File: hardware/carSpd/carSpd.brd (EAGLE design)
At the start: 68.5 x 32.5 mm, 66 parts, among them IC1 MCP16301/H, IC2 CP2102, IC3 DS3231/SO, Q1 2n3904, U1 ATMEGA328P_TQFP, U3 ERC1602-4SMD-LED, U4 DS1820, Y1 16mhz, Y2 16MHZ

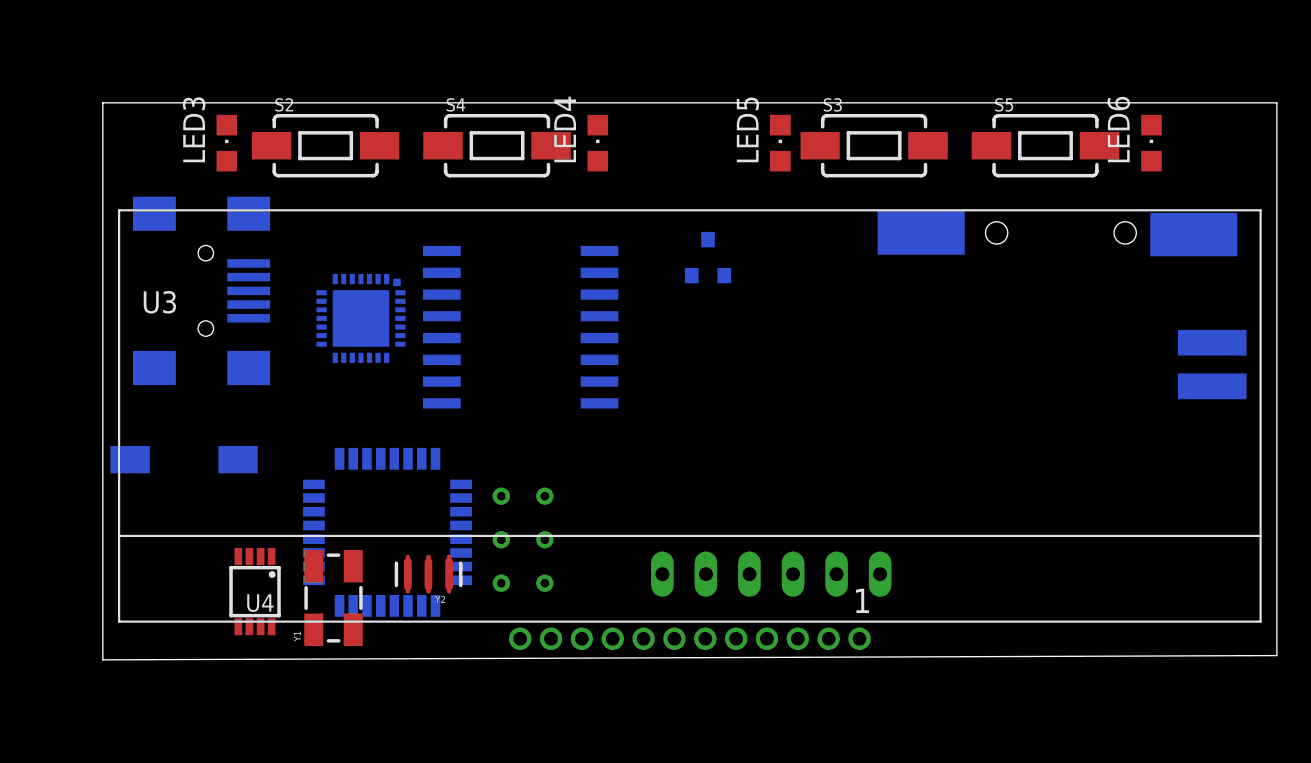
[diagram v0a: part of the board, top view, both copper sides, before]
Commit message: Corrected and verified schematics
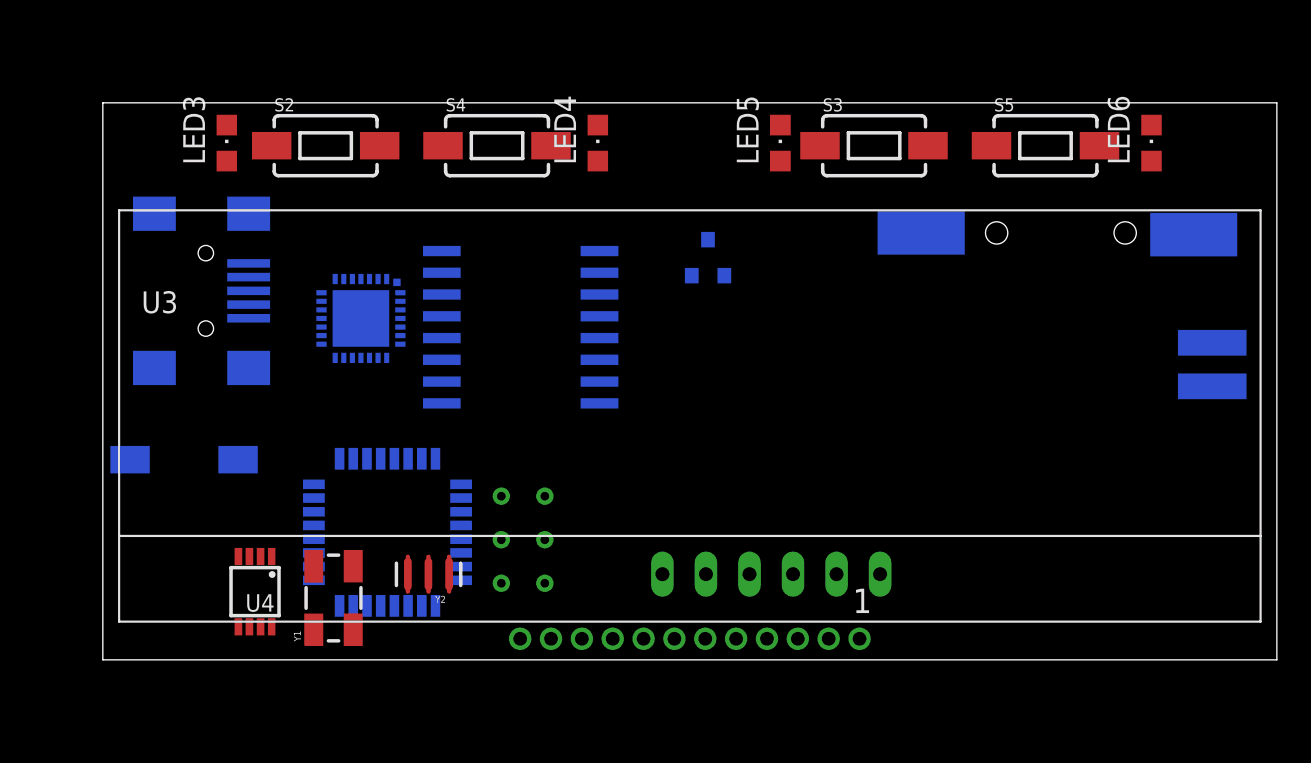
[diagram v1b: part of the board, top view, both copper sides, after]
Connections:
- removed net N$23: LED3.A, LED4.A, LED5.A, LED6.A, R15.1
- removed net N$25: C7.2, IC1.3, R8.1, R9.1
- new net N$1: IC1.3, R8.1, R9.1
- new net N$2: LED3.C, LED4.C, LED5.C, LED6.C, R15.1
- net +5V: now also LED3.A, LED4.A, LED5.A, LED6.A, U3.LED+
- net GND: now also C7.2; no longer LED3.C, LED4.C, LED5.C, LED6.C, U3.LED-
- net N$16: now also U3.LED-; no longer U3.LED+
- net TEMP: now also U1.14
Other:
- outline, holes or cut-outs redrawn
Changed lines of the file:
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@@
 <board>
 <plain>
-<wire x1="0" y1="0" x2="68.5" y2="0.25" width="0" layer="20"/>
-<wire x1="68.5" y1="0.25" x2="68.5" y2="32.5" width="0" layer="20"/>
+<wire x1="0" y1="0" x2="68.5" y2="0" width="0" layer="20"/>
+<wire x1="68.5" y1="0" x2="68.5" y2="32.5" width="0" layer="20"/>
 <wire x1="68.5" y1="32.5" x2="0" y2="32.5" width="0" layer="20"/>
 <wire x1="0" y1="32.5" x2="0" y2="0" width="0" layer="20"/>
@@
 <contactref element="C8" pad="2"/>
 <contactref element="U4" pad="4"/>
-<contactref element="LED3" pad="C"/>
-<contactref element="LED4" pad="C"/>
-<contactref element="LED5" pad="C"/>
-<contactref element="LED6" pad="C"/>
 <contactref element="IC3" pad="13"/>
 <contactref element="IC3" pad="5"/>
@@
 <contactref element="U3" pad="10"/>
 <contactref element="U3" pad="6"/>
-<contactref element="U3" pad="LED-"/>
 <contactref element="C4" pad="1"/>
 <contactref element="SV1" pad="6"/>
 <contactref element="IC1" pad="2"/>
-<contactref element="R8" pad="2"/>
 <contactref element="D4" pad="A"/>
 <contactref element="C5" pad="2"/>
@@
 <contactref element="D8" pad="A"/>
 <contactref element="U2" pad="1"/>
+<contactref element="C7" pad="2"/>
+<contactref element="R8" pad="2"/>
 <wire x1="-116" y1="-85" x2="-122" y2="-85" width="0" layer="19" extent="1-1"/>
 <wire x1="-110" y1="-85" x2="-116" y2="-85" width="0" layer="19" extent="1-1"/>
@@
 <wire x1="-101.85" y1="-70" x2="-104.3114" y2="-81.0988" width="0" layer="19" extent="1-1"/>
 <wire x1="-98.15" y1="-53" x2="-101.85" y2="-70" width="0" layer="19" extent="1-1"/>
-<wire x1="-99" y1="-36.15" x2="-98.15" y2="-53" width="0" layer="19" extent="1-1"/>
+<wire x1="-98.125" y1="-48" x2="-98.15" y2="-53" width="0" layer="19" extent="1-1"/>
+<wire x1="-99" y1="-36.15" x2="-98.125" y2="-48" width="0" layer="19" extent="1-1"/>
 <wire x1="-70.3" y1="-18.58" x2="-99" y2="-36.15" width="0" layer="19" extent="1-1"/>
 <wire x1="-56.18" y1="-13.42" x2="-70.3" y2="-18.58" width="0" layer="19" extent="1-1"/>
@@
 <wire x1="16.15" y1="30" x2="19.78" y2="23.855" width="0" layer="19" extent="1-16"/>
 <wire x1="8.51" y1="23.13" x2="15.06" y2="19.92" width="0" layer="19" extent="16-16"/>
-<wire x1="7.23" y1="31.2" x2="8.51" y2="23.13" width="0" layer="19" extent="1-16"/>
 <wire x1="26.15" y1="30" x2="19.78" y2="23.855" width="0" layer="19" extent="1-16"/>
-<wire x1="28.88" y1="31.2" x2="26.15" y2="30" width="0" layer="19" extent="1-1"/>
 <wire x1="28.98" y1="23.855" x2="26.15" y2="30" width="0" layer="19" extent="1-16"/>
 <wire x1="28.98" y1="22.585" x2="28.98" y2="23.855" width="0" layer="19" extent="16-16"/>
@@
 <wire x1="28.98" y1="18.775" x2="28.98" y2="20.045" width="0" layer="19" extent="16-16"/>
 <wire x1="34.36" y1="22.42" x2="28.98" y2="22.585" width="0" layer="19" extent="16-16"/>
-<wire x1="39.53" y1="31.2" x2="34.36" y2="22.42" width="0" layer="19" extent="1-16"/>
-<wire x1="48.15" y1="30" x2="39.53" y2="31.2" width="0" layer="19" extent="1-1"/>
+<wire x1="48.15" y1="30" x2="34.36" y2="22.42" width="0" layer="19" extent="1-16"/>
 <wire x1="58.15" y1="30" x2="48.15" y2="30" width="0" layer="19" extent="1-1"/>
-<wire x1="61.18" y1="31.2" x2="58.15" y2="30" width="0" layer="19" extent="1-1"/>
-<wire x1="63.65" y1="24.81" x2="61.18" y2="31.2" width="0" layer="19" extent="1-16"/>
-<wire x1="64.73" y1="15.96" x2="63.65" y2="24.81" width="0" layer="19" extent="16-16"/>
+<wire x1="63.65" y1="24.81" x2="58.15" y2="30" width="0" layer="19" extent="1-16"/>
 </signal>
 <signal name="+5V">
@@
 <contactref element="U2" pad="4"/>
 <contactref element="U2" pad="2"/>
+<contactref element="U3" pad="LED+"/>
+<contactref element="LED6" pad="A"/>
+<contactref element="LED3" pad="A"/>
+<contactref element="LED4" pad="A"/>
+<contactref element="LED5" pad="A"/>
 <wire x1="-102" y1="-74.901" x2="-102" y2="-81.0988" width="0" layer="19" extent="1-1"/>
 <wire x1="-105.85" y1="-70" x2="-102" y2="-74.901" width="0" layer="19" extent="1-1"/>
@@
 <wire x1="-68.5" y1="-2.07" x2="-70.325" y2="15.71" width="0" layer="19" extent="1-1"/>
 <wire x1="-74.69" y1="39.94" x2="-58.755" y2="31.4" width="0" layer="19" extent="1-1"/>
-<wire x1="8.51" y1="19.93" x2="-43.04" y2="20.87" width="0" layer="19" extent="1-16"/>
+<wire x1="7.23" y1="29.1" x2="-42.965" y2="31.03" width="0" layer="19" extent="1-1"/>
+<wire x1="8.51" y1="19.93" x2="7.23" y2="29.1" width="0" layer="19" extent="1-16"/>
 <wire x1="16.56" y1="17.62" x2="8.51" y2="19.93" width="0" layer="19" extent="16-16"/>
 <wire x1="17.36" y1="18.42" x2="16.56" y2="17.62" width="0" layer="19" extent="16-16"/>
@@
 <wire x1="44.15" y1="1.23" x2="42.35" y2="1.23" width="0" layer="19" extent="1-1"/>
 <wire x1="45.35" y1="5" x2="44.15" y2="1.23" width="0" layer="19" extent="1-1"/>
+<wire x1="28.88" y1="29.1" x2="17.36" y2="18.42" width="0" layer="19" extent="1-16"/>
+<wire x1="39.53" y1="29.1" x2="28.88" y2="29.1" width="0" layer="19" extent="1-1"/>
+<wire x1="61.18" y1="29.1" x2="39.53" y2="29.1" width="0" layer="19" extent="1-1"/>
+<wire x1="64.73" y1="18.5" x2="61.18" y2="29.1" width="0" layer="19" extent="1-16"/>
 </signal>
 <signal name="+12V">
@@
 <wire x1="-57.03" y1="9.81" x2="35.31" y2="24.52" width="0" layer="19" extent="1-1"/>
 </signal>
-<signal name="N$23">
-<contactref element="LED3" pad="A"/>
-<contactref element="LED6" pad="A"/>
-<contactref element="LED5" pad="A"/>
-<contactref element="LED4" pad="A"/>
-<contactref element="R15" pad="1"/>
-<wire x1="61.18" y1="29.1" x2="-100.04" y2="46.07" width="0" layer="19" extent="1-1"/>
-<wire x1="39.53" y1="29.1" x2="61.18" y2="29.1" width="0" layer="19" extent="1-1"/>
-<wire x1="28.88" y1="29.1" x2="39.53" y2="29.1" width="0" layer="19" extent="1-1"/>
-<wire x1="7.23" y1="29.1" x2="28.88" y2="29.1" width="0" layer="19" extent="1-1"/>
-</signal>
 <signal name="N$27">
 <contactref element="IC3" pad="14"/>
@@
 <contactref element="U4" pad="1"/>
 <contactref element="R16" pad="1"/>
+<contactref element="U1" pad="14"/>
 <wire x1="9.855" y1="6.03" x2="-100.04" y2="20.67" width="0" layer="19" extent="1-1"/>
+<wire x1="15.41" y1="3.1474" x2="9.855" y2="6.03" width="0" layer="19" extent="1-16"/>
 </signal>
 <signal name="N$24">
@@
 </signal>
 <signal name="N$16">
-<contactref element="U3" pad="LED+"/>
 <contactref element="R14" pad="1"/>
-<wire x1="-58.73" y1="9.81" x2="64.73" y2="18.5" width="0" layer="19" extent="1-16"/>
+<contactref element="U3" pad="LED-"/>
+<wire x1="-58.73" y1="9.81" x2="64.73" y2="15.96" width="0" layer="19" extent="1-16"/>
 </signal>
 <signal name="N$18">
@@
 <wire x1="-99.95" y1="-36.15" x2="-98.125" y2="-63" width="0" layer="19" extent="1-1"/>
 </signal>
-<signal name="N$25">
-<contactref element="R8" pad="1"/>
+<signal name="N$2">
+<contactref element="R15" pad="1"/>
+<contactref element="LED3" pad="C"/>
+<contactref element="LED4" pad="C"/>
+<contactref element="LED5" pad="C"/>
+<contactref element="LED6" pad="C"/>
+<wire x1="39.53" y1="31.2" x2="61.18" y2="31.2" width="0" layer="19" extent="1-1"/>
+<wire x1="28.88" y1="31.2" x2="39.53" y2="31.2" width="0" layer="19" extent="1-1"/>
+<wire x1="7.23" y1="31.2" x2="28.88" y2="31.2" width="0" layer="19" extent="1-1"/>
+<wire x1="-100.04" y1="46.07" x2="7.23" y2="31.2" width="0" layer="19" extent="1-1"/>
+</signal>
+<signal name="N$1">
 <contactref element="IC1" pad="3"/>
 <contactref element="R9" pad="1"/>
-<contactref element="C7" pad="2"/>
+<contactref element="R8" pad="1"/>
 <wire x1="-99.85" y1="-53" x2="-99.85" y2="-58" width="0" layer="19" extent="1-1"/>
-<wire x1="-98.125" y1="-48" x2="-99.85" y2="-53" width="0" layer="19" extent="1-1"/>
-<wire x1="-98.05" y1="-36.15" x2="-98.125" y2="-48" width="0" layer="19" extent="1-1"/>
+<wire x1="-98.05" y1="-36.15" x2="-99.85" y2="-53" width="0" layer="19" extent="1-1"/>
 </signal>
 </signals>

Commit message: Routing complete
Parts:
- added H1, H2, H3, H4: STAND-OFF, SparkFun-Hardware:STAND-OFF
- C6: value 100nf -> 0.1uf
- L1: device rcl:L3225M -> hybridair:IND-1007/2518
- SV1: device con-lsta:FE06W -> con-lsta:FE05W
- U4: value DS1820 -> (none)
- moved C5 180.9 mm to (49.9, 2.92), flipped to the bottom, turned to 270 degrees
- moved U2 177.9 mm to (54.0, 7.62), flipped to the bottom
- moved D8 177.3 mm to (29.6, 3.56), flipped to the bottom, turned to 180 degrees
- moved D7 174.7 mm to (27.7, 11.4), flipped to the bottom, turned to 180 degrees
- moved D4 173.2 mm to (49.8, 11.7), flipped to the bottom, turned to 90 degrees
- moved D5 173.2 mm to (48.6, 6.10), flipped to the bottom
- moved C6 171.8 mm to (56.8, 9.53), flipped to the bottom, turned to 270 degrees
- moved R9 170.5 mm to (59.7, 4.32), flipped to the bottom, turned to 270 degrees
- moved R8 169.9 mm to (59.7, 7.62), flipped to the bottom, turned to 90 degrees
- moved D6 167.8 mm to (27.7, 8.00), flipped to the bottom, turned to 180 degrees
- moved L1 165.8 mm to (48.6, 8.38), flipped to the bottom
- moved IC1 158.8 mm to (54.0, 7.62), flipped to the bottom, turned to 270 degrees
- moved C7 158.7 mm to (48.0, 11.6), flipped to the bottom, turned to 90 degrees
- moved R16 135.2 mm to (35.9, 26.4), flipped to the bottom
- moved R15 126.1 mm to (24.1, 19.3), flipped to the bottom
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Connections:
- removed net N$28: S2.1, U1.10
- removed net N$29: LED2.A, R12.1
- removed net N$33: S3.1, U1.12
- removed net N$34: S4.1, U1.11
- removed net N$35: S5.1, U1.13
- new net N$13: S5.1, U1.2
- new net N$3: LED2.C, R12.1
- new net N$5: S2.1, U1.24
- new net N$6: S4.1, U1.25
- new net N$7: S3.1, U1.26
- net +12V: now also SV1.1; no longer SV1.2
- net +5V: now also L1.P$2, LED2.A; no longer L1.2, R12.2, SV1.1
- net GND: now also R12.2, SV1.5; no longer LED2.C, SV1.6
- net INJ: now also SV1.3; no longer SV1.4
- net LIGHTING: now also SV1.4; no longer SV1.5
- net N$18: now also L1.P$1; no longer L1.1
- net VSS: now also SV1.2; no longer SV1.3
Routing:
- net +5V: track 0.00 -> 251.4 mm, vias 0 -> 13
- net N$2: track 0.00 -> 70.0 mm, vias 0 -> 1
- net SDA: track 0.00 -> 54.8 mm, vias 0 -> 3
- net SCL: track 0.00 -> 50.1 mm, vias 0 -> 3
- net TEMP: track 0.00 -> 45.8 mm, vias 0 -> 2
- net N$13: track 0.00 -> 45.4 mm, vias 0 -> 1
- net N$15: track 0.00 -> 39.9 mm, vias 0 -> 2
- net N$7: track 0.00 -> 35.6 mm, vias 0 -> 1
- net N$31: track 0.00 -> 29.9 mm, vias 0 -> 3
- net RST: track 0.00 -> 29.8 mm, vias 0 -> 2
- net LED_PWM: track 0.00 -> 26.0 mm, vias 0 -> 2
- net N$27: track 0.00 -> 24.4 mm, vias 0 -> 2
- net N$36: track 0.00 -> 20.7 mm, vias 0 -> 2
- net INJ: track 0.00 -> 19.4 mm
- net N$5: track 0.00 -> 16.7 mm, vias 0 -> 1
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- added copper zone on layer 1, net GND
- added copper zone on layer 16, net GND
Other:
- board size 68.5 x 32.5 mm -> 168.3 x 34.8 mm

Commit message: Finished optimizations
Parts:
- moved R2 26.4 mm to (29.2, 16.8), flipped to the bottom, turned to 0 degrees
- moved R12 24.9 mm to (29.2, 15.2), flipped to the bottom, turned to 180 degrees
- moved LED1 23.2 mm to (29.2, 18.4)
- moved LED2 21.7 mm to (29.2, 13.6), turned to 270 degrees
- moved C15 6.61 mm to (47.4, 2.03), turned to 180 degrees
- moved R15 1.02 mm to (23.1, 19.3)
- moved R1 0.52 mm to (11.3, 3.30)
- moved Y2 0.13 mm to (20.8, 3.30)
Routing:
- net +5V: track 251.4 -> 274.4 mm, vias 13 -> 14
- net N$26: track 10.0 -> 29.0 mm, vias 1 -> 3
- net N$3: track 13.6 -> 1.73 mm, vias 1 -> 0
- net N$32: track 10.5 -> 1.73 mm, vias 1 -> 0
- net N$31: track 29.9 -> 26.1 mm
- net N$5: track 16.7 -> 15.6 mm
- net SDA: track 54.8 -> 53.9 mm
- net N$15: track 39.9 -> 40.8 mm
- net N$6: track 15.6 -> 14.8 mm
- net LED_PWM: track 26.0 -> 26.8 mm
- net SCL: track 50.1 -> 49.4 mm
- net TEMP: track 45.8 -> 46.6 mm
- net N$7: track 35.6 -> 36.2 mm
- net GND: vias 16 -> 20

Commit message: PCB design complete
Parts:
- added LED7, LED8: (no value), led:CHIPLED_0805
- added U$1: (no value), ar1logo:AR1
- added U$2: (no value), ar1logo:CARSPD
- moved C8 3.56 mm to (10.0, 31.6)
- moved LED5 2.39 mm to (38.5, 30.1)
- moved S3 2.39 mm to (44.2, 30.1)
- moved C10 2.30 mm to (9.02, 29.3), turned to 0 degrees
- moved LED4 2.16 mm to (29.8, 30.1)
- moved S4 2.16 mm to (24.1, 30.1)
- moved B1 1.27 mm to (55.8, 25.1)
- moved C11 1.02 mm to (19.4, 18.1)
- moved C3 1.02 mm to (11.9, 17.4)
- moved H2 1.02 mm to (65.4, 30.1)
- moved H3 1.02 mm to (3.17, 30.1)
- moved IC2 1.02 mm to (16.5, 22.6)
- moved LED1 1.02 mm to (29.2, 19.4)
- moved LED3 1.02 mm to (6.99, 30.1)
- moved LED6 1.02 mm to (61.6, 30.1)
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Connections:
- net +5V: now also LED7.A, LED8.A
- net N$2: now also LED7.C, LED8.C
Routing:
- net +5V: track 274.4 -> 279.4 mm, vias 14 -> 15
- net N$12: track 12.5 -> 11.3 mm
- net SDA: track 53.9 -> 53.0 mm
- net N$2: track 70.2 -> 71.0 mm
- net N$27: track 24.4 -> 23.8 mm
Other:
- board size 168.3 x 34.8 mm -> 68.6 x 33.4 mm
- board text added: "ICSP"
- board text added: "PWR"
- board text added: "STAT"
- board text added: "Version 0.1 carspd.hybridair.me Blake Stratton 07.11.2017"
